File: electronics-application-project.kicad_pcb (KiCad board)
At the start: 2 copper layers, 54 parts, among them J1 Conn_02x03_Odd_Even, J2 Conn_01x02_Pin, J3 Conn_01x02_Pin, J4 Conn_01x02_Pin, U1 W5500, U2 ARJM11C7-114-BA-EW2, U3 LM2574-3.3YN, U4 ATTINY85-20SU, U5 74HC00, Y2 ABLS7M2-25.000MHZ-D-2Y-T

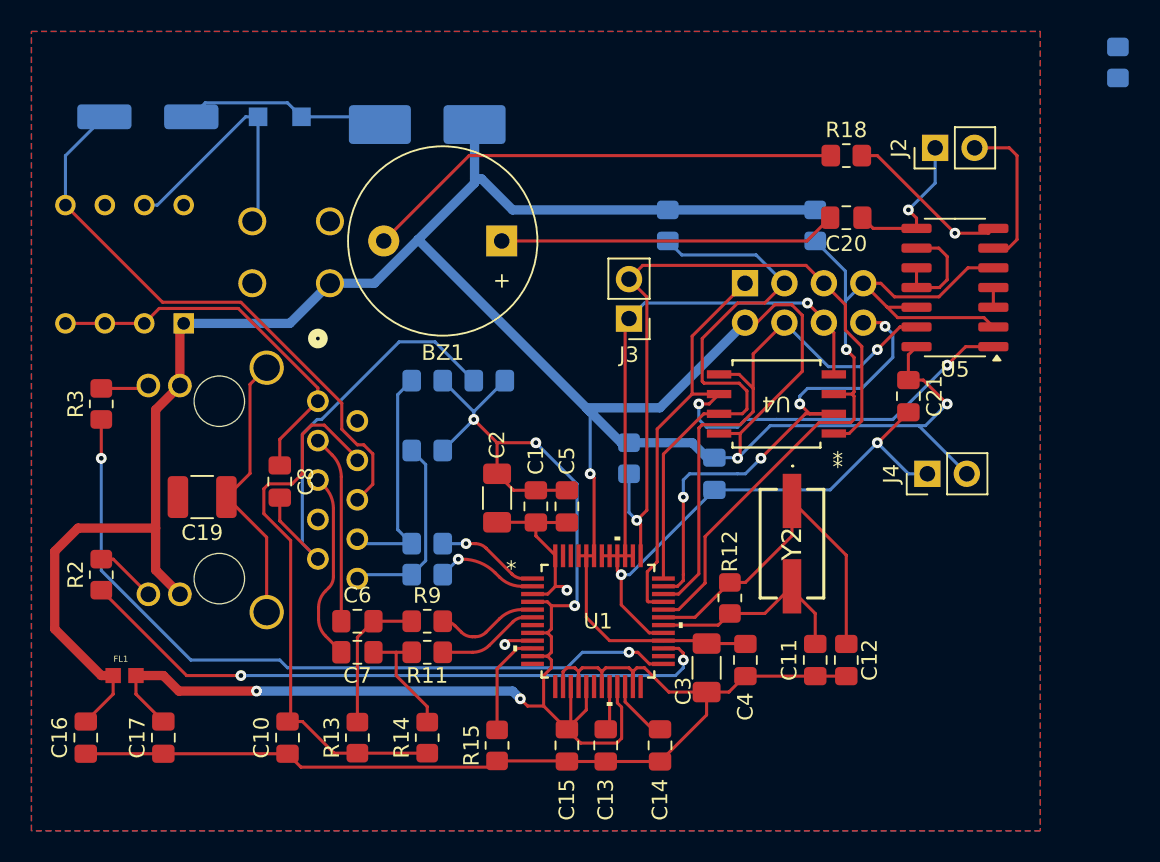
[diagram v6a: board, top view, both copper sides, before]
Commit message: flip buzzer to back side
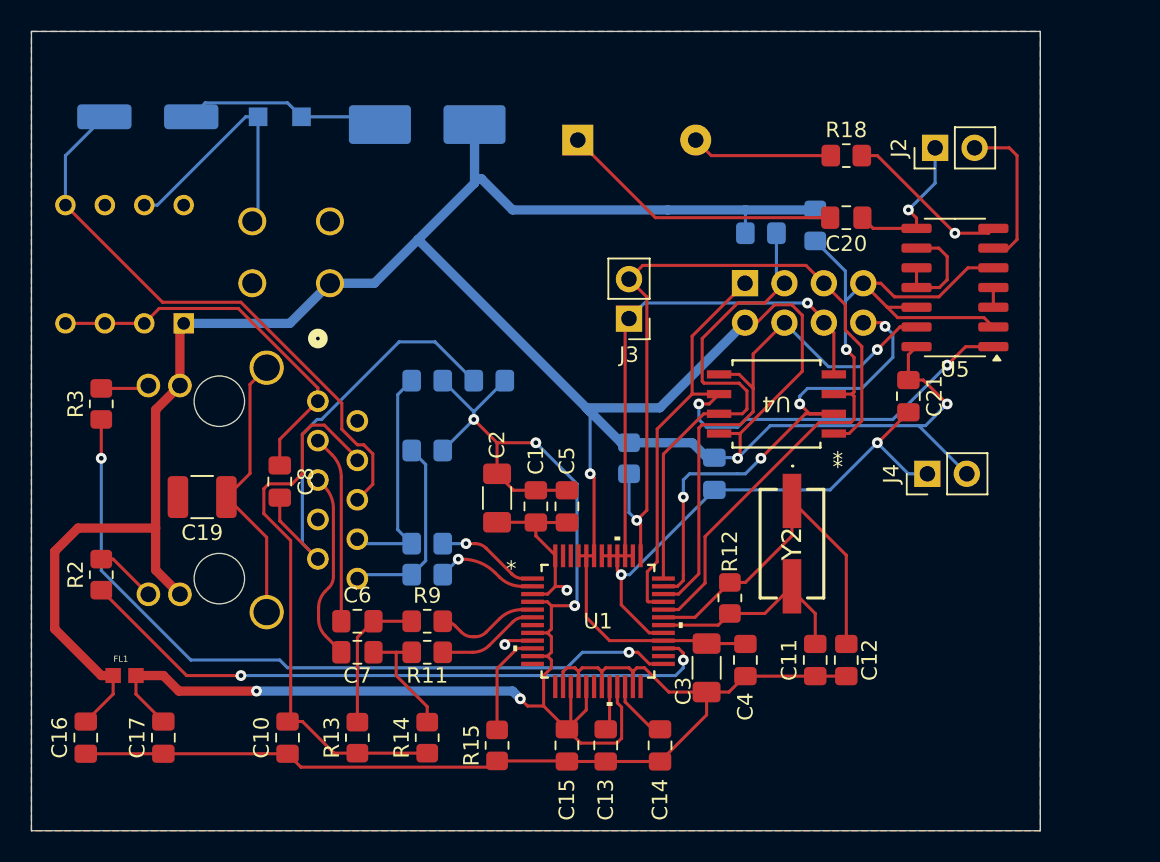
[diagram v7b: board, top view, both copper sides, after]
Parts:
- removed R16: 4.7K, Resistor_SMD:R_0805_2012Metric_Pad1.20x1.40mm_HandSolder
- BZ1: moved to B.Cu
- moved BZ1 8.14 mm to (150.7, 83.5), turned to 0 degrees
- moved R1 6.02 mm to (162.5, 89.5), turned to 180 degrees
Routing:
- net Net-(BZ1--): track 31.1 -> 9.11 mm
- net /INTn: track 37.1 -> 31.9 mm
- net Net-(BZ1-+): track 21.8 -> 18.3 mm
- net 3.3V_D: track 195.2 -> 196.7 mm
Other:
- board outline added: 65 x 51.5 mm

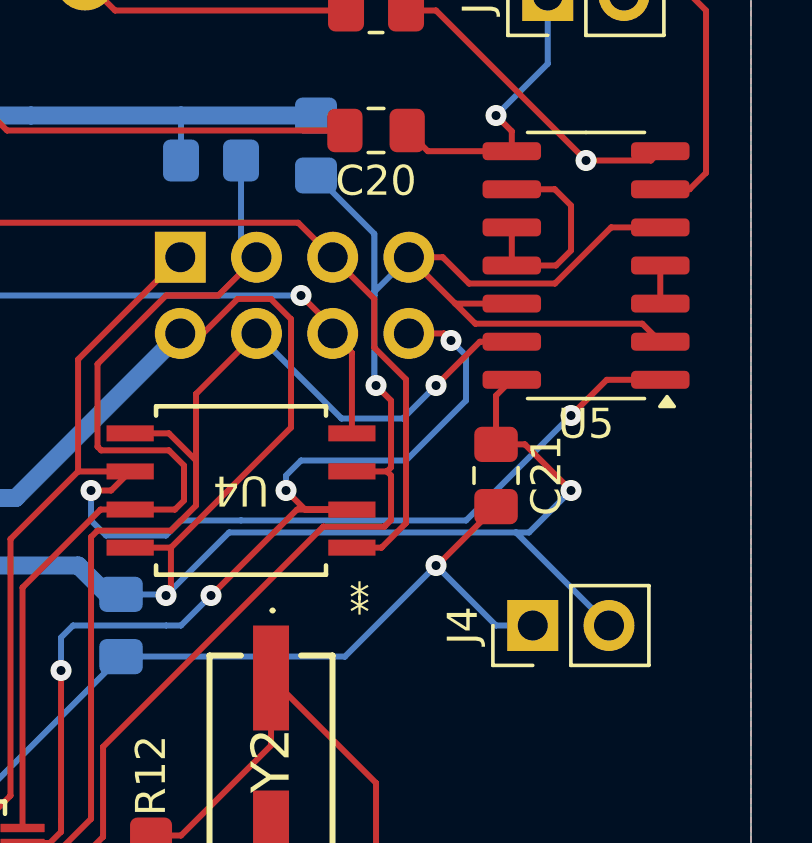
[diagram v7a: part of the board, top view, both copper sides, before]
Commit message: gnd issue fixed
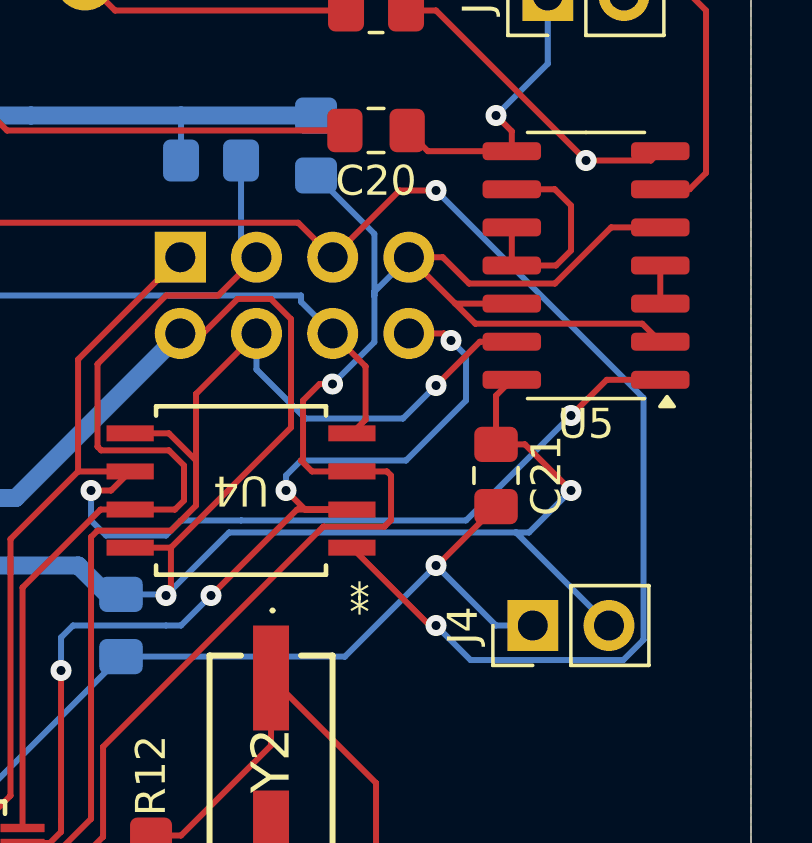
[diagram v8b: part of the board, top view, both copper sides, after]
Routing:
- net /RSTn: track 47.3 -> 69.0 mm, vias 1 -> 3
- net /SCSn: track 55.6 -> 58.1 mm
- net /MISO: track 36.0 -> 36.7 mm
- net GND: track 198.5 -> 199.1 mm, vias 6 -> 5
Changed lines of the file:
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@@
 			(keep_text_aligned yes)
 		)
-		(gr_text "65.0000 mm"
+		(gr_text "65,0000 mm"
 			(at 148 71.2 0)
 			(layer "F.Cu")
@@
 			(keep_text_aligned yes)
 		)
-		(gr_text "51.5000 mm"
+		(gr_text "51,5000 mm"
 			(at 108.7 102.25 90)
 			(layer "F.Cu")
@@
 	)
 	(segment
-		(start 168.5 97.5)
-		(end 168.5 99.73)
-		(width 0.2)
-		(layer "F.Cu")
-		(net 2)
-	)
-	(segment
 		(start 171.309 94.939)
 		(end 176.874 94.939)
@@
 	)
 	(segment
-		(start 167.1957 99.865)
-		(end 168.365 99.865)
-		(width 0.2)
-		(layer "F.Cu")
-		(net 2)
-	)
-	(segment
 		(start 170.64 94.27)
 		(end 171.309 94.939)
@@
 	)
 	(segment
-		(start 168 97)
-		(end 168.5 97.5)
+		(start 166.2419 101.7027)
+		(end 158.901 109.0436)
 		(width 0.2)
 		(layer "F.Cu")
@@
 	)
 	(segment
-		(start 166.2419 101.7027)
-		(end 158.901 109.0436)
+		(start 168.2841 101.7027)
+		(end 166.2419 101.7027)
 		(width 0.2)
 		(layer "F.Cu")
@@
 	)
 	(segment
-		(start 168.2841 101.7027)
-		(end 166.2419 101.7027)
+		(start 166.116265 96.950735)
+		(end 166.549265 96.950735)
 		(width 0.2)
 		(layer "F.Cu")
@@
 	)
 	(segment
+		(start 168.365 99.865)
+		(end 167.1957 99.865)
+		(width 0.2)
+		(layer "F.Cu")
+		(net 2)
+	)
+	(segment
 		(start 168.5 100)
 		(end 168.5 101.4868)
@@
 	)
 	(segment
+		(start 167.1957 99.865)
+		(end 165.865 99.865)
+		(width 0.2)
+		(layer "F.Cu")
+		(net 2)
+	)
+	(segment
+		(start 165.865 99.865)
+		(end 165.5 99.5)
+		(width 0.2)
+		(layer "F.Cu")
+		(net 2)
+	)
+	(segment
 		(start 171.101 93.601)
 		(end 170.225 92.725)
@@
 	)
 	(segment
+		(start 165.5 99.5)
+		(end 165.567 99.433)
+		(width 0.2)
+		(layer "F.Cu")
+		(net 2)
+	)
+	(segment
 		(start 175.8371 91.73)
 		(end 173.9661 93.601)
@@
 	)
 	(segment
-		(start 168.5 99.73)
-		(end 168.365 99.865)
+		(start 165.567 99.433)
+		(end 165.567 97.5)
 		(width 0.2)
 		(layer "F.Cu")
@@
 		(net 2)
 	)
+	(segment
+		(start 165.567 97.5)
+		(end 166.116265 96.950735)
+		(width 0.2)
+		(layer "F.Cu")
+		(net 2)
+	)
 	(via
-		(at 168 97)
+		(at 166.549265 96.950735)
 		(size 0.7)
 		(drill 0.3)
@@
 	)
 	(segment
-		(start 167.944 96.944)
-		(end 168 97)
+		(start 166.549265 96.950735)
+		(end 167.944 95.556)
 		(width 0.2)
 		(layer "B.Cu")
@@
 	)
 	(segment
-		(start 167.944 94)
-		(end 167.944 96.944)
+		(start 167.944 95.556)
+		(end 167.944 94)
 		(width 0.2)
 		(layer "B.Cu")
@@
 	(segment
 		(start 167.1957 102.405)
-		(end 168.1831 102.405)
+		(end 169.7907 105)
 		(width 0.2)
 		(layer "F.Cu")
@@
 	)
 	(segment
-		(start 154.5 108)
-		(end 155.151 107.349)
+		(start 169.7907 105)
+		(end 170 105)
 		(width 0.2)
 		(layer "F.Cu")
@@
 	)
 	(segment
-		(start 167.944 94.114)
-		(end 166.555 92.725)
+		(start 154.5 108)
+		(end 155.151 107.349)
 		(width 0.2)
 		(layer "F.Cu")
@@
 	)
 	(segment
-		(start 168.1831 102.405)
-		(end 169 101.5881)
+		(start 168.78 90.5)
+		(end 166.555 92.725)
 		(width 0.2)
 		(layer "F.Cu")
@@
 	)
 	(segment
-		(start 169 96.79776)
-		(end 167.944 95.74176)
+		(start 166.555 92.725)
+		(end 165.404 91.574)
 		(width 0.2)
 		(layer "F.Cu")
@@
 	)
 	(segment
-		(start 169 101.5881)
-		(end 169 96.79776)
+		(start 165.404 91.574)
+		(end 154.886 91.574)
 		(width 0.2)
 		(layer "F.Cu")
@@
 	)
 	(segment
-		(start 167.944 95.74176)
-		(end 167.944 94.114)
+		(start 170 90.5)
+		(end 168.78 90.5)
 		(width 0.2)
 		(layer "F.Cu")
 		(net 4)
 	)
-	(segment
-		(start 166.555 92.725)
-		(end 165.404 91.574)
-		(width 0.2)
-		(layer "F.Cu")
+	(via
+		(at 154.5 108)
+		(size 0.7)
+		(drill 0.3)
+		(layers "F.Cu" "B.Cu")
 		(net 4)
 	)
-	(segment
-		(start 165.404 91.574)
-		(end 154.886 91.574)
-		(width 0.2)
-		(layer "F.Cu")
+	(via
+		(at 170 105)
+		(size 0.7)
+		(drill 0.3)
+		(layers "F.Cu" "B.Cu")
 		(net 4)
 	)
 	(via
-		(at 154.5 108)
+		(at 170 90.5)
 		(size 0.7)
 		(drill 0.3)
@@
 	)
 	(segment
+		(start 176.916 105.47676)
+		(end 176.916 97.416)
+		(width 0.2)
+		(layer "B.Cu")
+		(net 4)
+	)
+	(segment
+		(start 171.151 106.151)
+		(end 176.24176 106.151)
+		(width 0.2)
+		(layer "B.Cu")
+		(net 4)
+	)
+	(segment
+		(start 176.916 97.416)
+		(end 170 90.5)
+		(width 0.2)
+		(layer "B.Cu")
+		(net 4)
+	)
+	(segment
+		(start 170 105)
+		(end 171.151 106.151)
+		(width 0.2)
+		(layer "B.Cu")
+		(net 4)
+	)
+	(segment
 		(start 154.5 108)
 		(end 154 107.5)
@@
 	)
 	(segment
+		(start 176.24176 106.151)
+		(end 176.916 105.47676)
+		(width 0.2)
+		(layer "B.Cu")
+		(net 4)
+	)
+	(segment
 		(start 154 107.5)
 		(end 154 105)
@@
 	)
 	(segment
+		(start 167.651 98.1397)
+		(end 167.651 96.361)
+		(width 0.2)
+		(layer "F.Cu")
+		(net 5)
+	)
+	(segment
 		(start 124 123.0375)
 		(end 132 123.0375)
@@
 	)
 	(segment
+		(start 167.1957 98.595)
+		(end 167.651 98.1397)
+		(width 0.2)
+		(layer "F.Cu")
+		(net 5)
+	)
+	(segment
 		(start 149.9625 123.5)
 		(end 150 123.5375)
@@
 	)
 	(segment
-		(start 166.555 95.055)
-		(end 165.5 94)
-		(width 0.2)
-		(layer "F.Cu")
-		(net 5)
-	)
-	(segment
 		(start 154.250001 117.749999)
 		(end 154.250001 118.7164)
@@
 	)
 	(segment
+		(start 167.651 96.361)
+		(end 166.555 95.265)
+		(width 0.2)
+		(layer "F.Cu")
+		(net 5)
+	)
+	(segment
 		(start 160.4375 119.0625)
 		(end 159 119.0625)
@@
 	)
 	(segment
-		(start 167.1957 95.9057)
-		(end 166.555 95.265)
-		(width 0.2)
-		(layer "F.Cu")
-		(net 5)
-	)
-	(segment
 		(start 152.25 117.75)
 		(end 152.5 117.5)
@@
 		(net 5)
 	)
-	(segment
-		(start 167.1957 98.595)
-		(end 167.1957 95.9057)
-		(width 0.2)
-		(layer "F.Cu")
-		(net 5)
-	)
 	(via
 		(at 150 112.5)
@@
 	)
 	(via
-		(at 165.5 94)
-		(size 0.7)
-		(drill 0.3)
-		(layers "F.Cu" "B.Cu")
-		(net 5)
-	)
-	(via
 		(at 153.5 111.5)
 		(size 0.7)
@@
 	)
 	(segment
+		(start 165.5 94)
+		(end 165.5 94.21)
+		(width 0.2)
+		(layer "B.Cu")
+		(net 5)
+	)
+	(segment
 		(start 166.9625 106.0375)
 		(end 159.5 106.0375)
@@
 	)
 	(segment
+		(start 165.5 94.21)
+		(end 166.555 95.265)
+		(width 0.2)
+		(layer "B.Cu")
+		(net 5)
+	)
+	(segment
 		(start 172 105)
 		(end 170 103)
@@
 	)
 	(segment
-		(start 168.899 98.101)
-		(end 166.851 98.101)
+		(start 165.648919 98.101)
+		(end 164.015 96.467081)
+		(width 0.2)
+		(layer "B.Cu")
+		(net 38)
+	)
+	(segment
+		(start 164.015 96.467081)
+		(end 164.015 95.265)
 		(width 0.2)
 		(layer "B.Cu")
@@
 	)
 	(segment
-		(start 166.851 98.101)
-		(end 164.015 95.265)
+		(start 168.899 98.101)
+		(end 165.648919 98.101)
 		(width 0.2)
 		(layer "B.Cu")
